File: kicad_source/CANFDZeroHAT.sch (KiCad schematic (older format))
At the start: 31 parts, among them CN1 RASPI-IO, CN2 691322310004, CN3 GH_SM04B-GHS-TB, CN4 GH_SM04B-GHS-TB, SW1 JS202011JCQN, U1 MCP2518FD, U2 TCAN332GDR, Y1 RH100-20.000-20-3030-TR

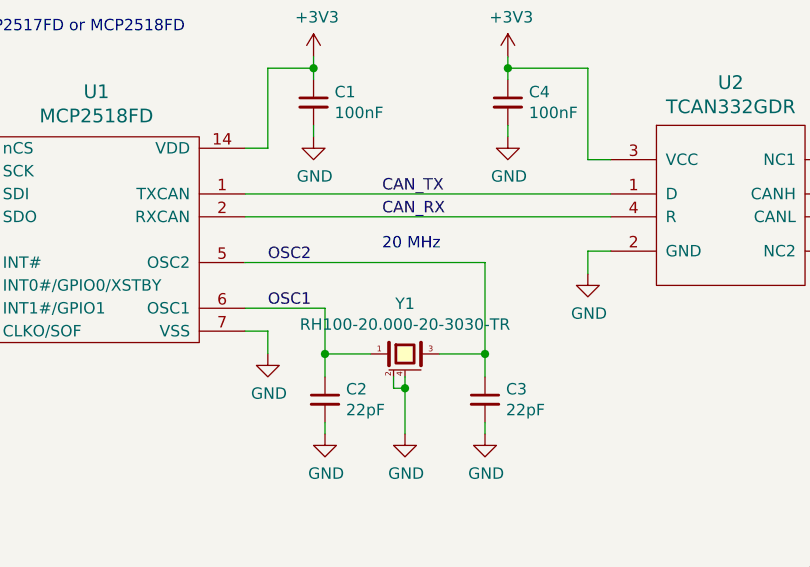
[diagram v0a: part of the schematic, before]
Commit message: updated 40 MHz crystal
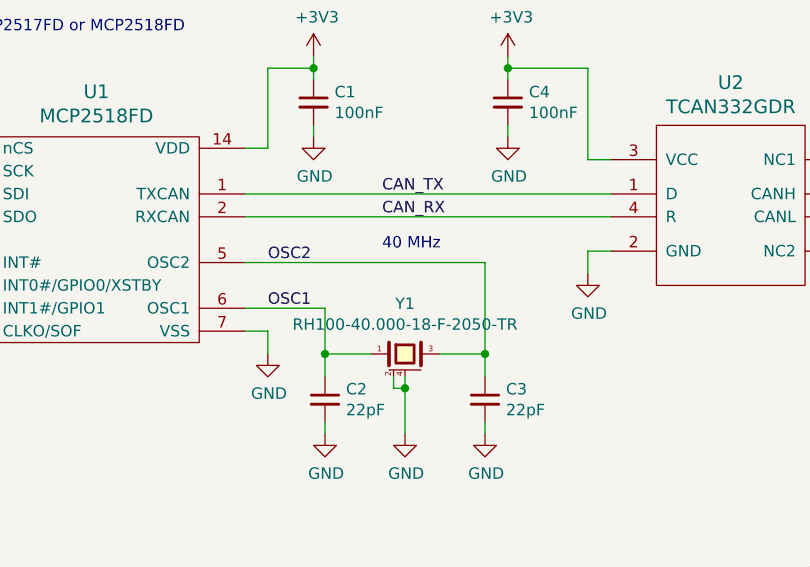
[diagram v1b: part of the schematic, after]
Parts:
- Y1: value RH100-20.000-20-3030-TR -> RH100-40.000-18-F-2050-TR
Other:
- note added: "40 MHz"
- note removed: "20 MHz"
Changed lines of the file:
@@
 AR Path="/5FD751A0" Ref="Y1"  Part="1"
 F 0 "Y1" H 3350 2520 50  0000 C CNN
-F 1 "RH100-20.000-20-3030-TR" H 3350 2429 50  0000 C CNN
+F 1 "RH100-40.000-18-F-2050-TR" H 3350 2429 50  0000 C CNN
 F 2 "crystals:Crystal_SMD_3.2x2.5mm_4Pad" H 3350 2100 50  0001 C CNN
 F 3 "" H 3350 2300 50  0000 C CNN
@@
 	9050 1300 9900 1300
 Text Notes 3250 1850 0    50   ~ 0
-20 MHz
+40 MHz
 $Comp
 L devices:Label L?

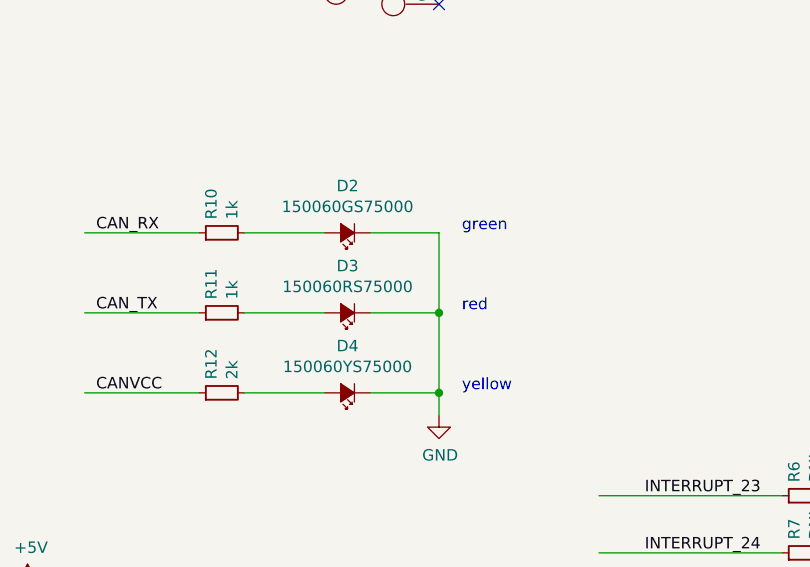
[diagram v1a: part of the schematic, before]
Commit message: made debug leds low active
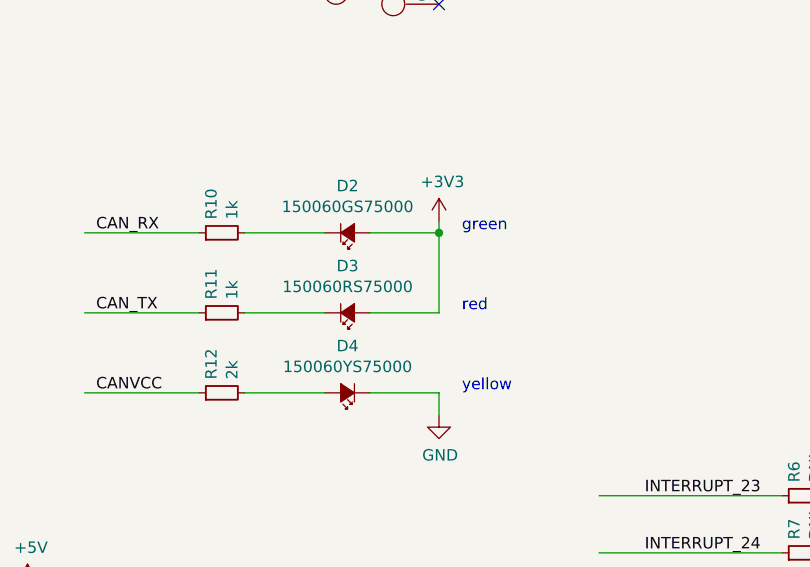
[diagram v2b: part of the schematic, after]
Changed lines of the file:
@@
 F 3 "" V 6200 3300 50  0000 C CNN
 	1    6200 3300
-	-1   0    0    1
+	1    0    0    1
 $EndComp
 $Comp
@@
 F 3 "" V 6200 3650 50  0000 C CNN
 	1    6200 3650
-	-1   0    0    1
+	1    0    0    1
 $EndComp
 $Comp
@@
 Wire Wire Line
 	6300 3650 6600 3650
-Connection ~ 6600 3650
-Wire Wire Line
-	6600 3650 6600 4000
 Wire Wire Line
 	6300 4000 6600 4000
-Connection ~ 6600 4000
 Wire Wire Line
 	6600 4000 6600 4100
@@
 Text Label 5100 4000 0    50   ~ 0
 CANVCC
+$Comp
+L power-supply:+3V3 #PWR?
+U 1 1 600FB023
+P 6600 3250
+AR Path="/5FD58A5B/600FB023" Ref="#PWR?"  Part="1"
+AR Path="/600FB023" Ref="#PWR?"  Part="1"
+F 0 "#PWR?" H 6600 3100 50  0001 C CNN
+F 1 "+3V3" H 6615 3423 50  0000 C CNN
+F 2 "" H 6600 3250 50  0000 C CNN
+F 3 "" H 6600 3250 50  0000 C CNN
+	1    6600 3250
+	1    0    0    -1
+$EndComp
+Wire Wire Line
+	6600 3300 6600 3250
+Connection ~ 6600 3300
 $EndSCHEMATC

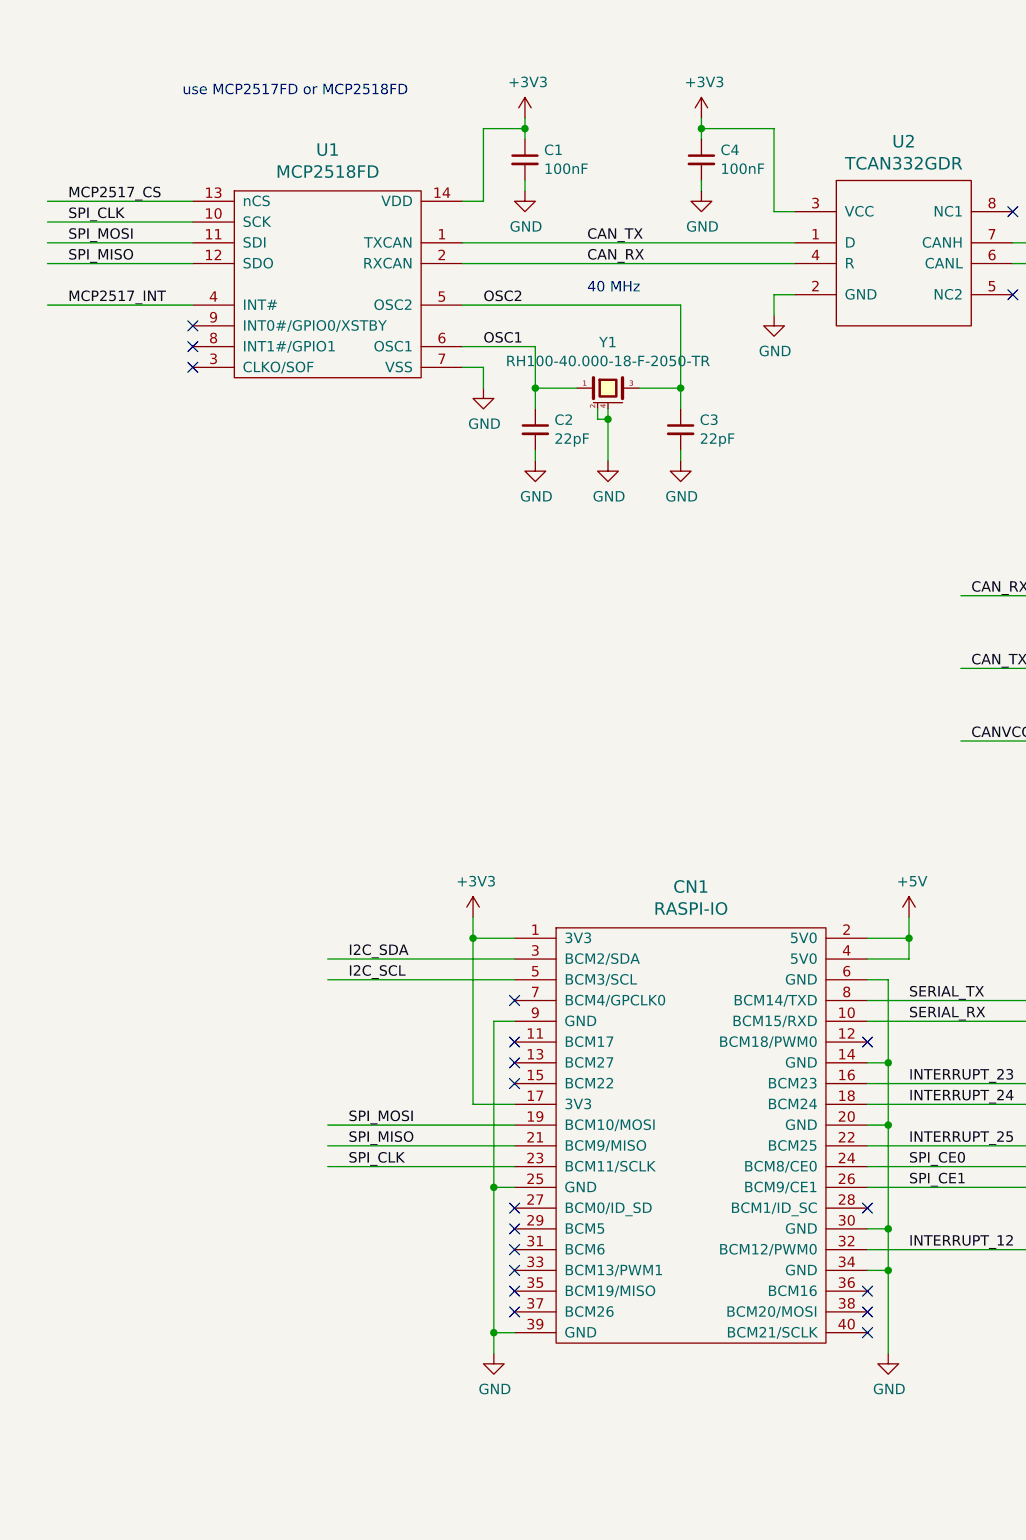
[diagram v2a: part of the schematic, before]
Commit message: updated labels
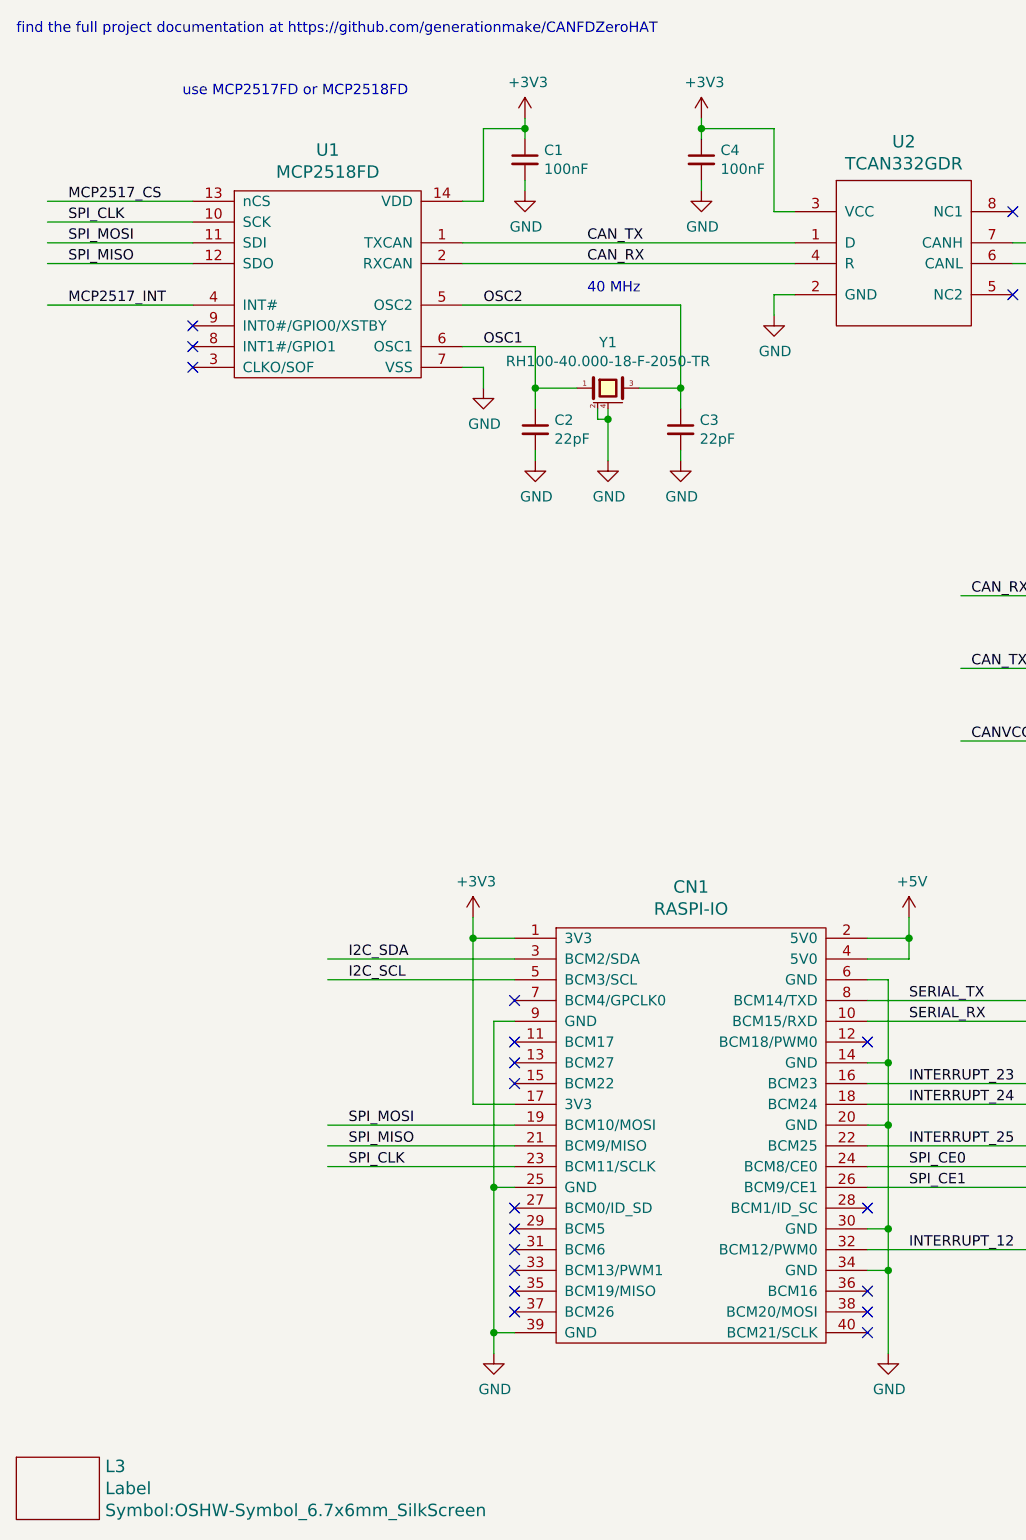
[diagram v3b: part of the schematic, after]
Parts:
- added L3: Label, Symbol:OSHW-Symbol_6.7x6mm_SilkScreen, symbol devices:Label
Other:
- note added: "find the full project documentation at https://github.com/generationmake/CANFDZeroHAT"
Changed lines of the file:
@@
 Sheet 1 1
 Title "CANFDZeroHAT"
-Date "2021-01-02"
+Date "2021-01-26"
 Rev "0.2"
 Comp "generationmake"
@@
 P 6600 3250
 AR Path="/5FD58A5B/600FB023" Ref="#PWR?"  Part="1"
-AR Path="/600FB023" Ref="#PWR?"  Part="1"
-F 0 "#PWR?" H 6600 3100 50  0001 C CNN
+AR Path="/600FB023" Ref="#PWR018"  Part="1"
+F 0 "#PWR018" H 6600 3100 50  0001 C CNN
 F 1 "+3V3" H 6615 3423 50  0000 C CNN
 F 2 "" H 6600 3250 50  0000 C CNN
@@
 	6600 3300 6600 3250
 Connection ~ 6600 3300
+$Comp
+L devices:Label L?
+U 1 1 60100FB3
+P 700 7600
+AR Path="/5FD58A5B/60100FB3" Ref="L?"  Part="1"
+AR Path="/60100FB3" Ref="L3"  Part="1"
+F 0 "L3" H 928 7706 60  0000 L CNN
+F 1 "Label" H 928 7600 60  0000 L CNN
+F 2 "Symbol:OSHW-Symbol_6.7x6mm_SilkScreen" H 928 7494 60  0000 L CNN
+F 3 "" H 700 7600 60  0000 C CNN
+	1    700  7600
+	1    0    0    -1
+$EndComp
+Text Notes 500  600  0    50   ~ 0
+find the full project documentation at https://github.com/generationmake/CANFDZeroHAT
 $EndSCHEMATC
